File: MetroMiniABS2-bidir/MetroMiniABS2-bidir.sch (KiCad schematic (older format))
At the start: 33 parts, among them CON1 PJ_037A, IC1 MCT6H, J1 RJ45, J2 RJ45, P1 Termination, P2 + 12V (IN) -, P3 In Track Out, P5 - 12V (out) +, SW1 Blue, SW2 Gold, U1 METROMINI, U2 MCP2517, U3 MCP2551, X1 20 Mhz

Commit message: Bidirection (two signals) version of MetroMiniABS2
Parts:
- added P4: CONN_8, ~, symbol CONN_8
- added R1, R13, R14, R6, R7, R8: 330 Ohms, ~, symbol R
- added R15: 10K, ~, symbol R
- added U4: TLC59208F, symbol TLC59208F
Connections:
- wire segments 132 -> 173
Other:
- moved on the sheet: D4, D5, R10, R11, R12, R9, SW1, SW2

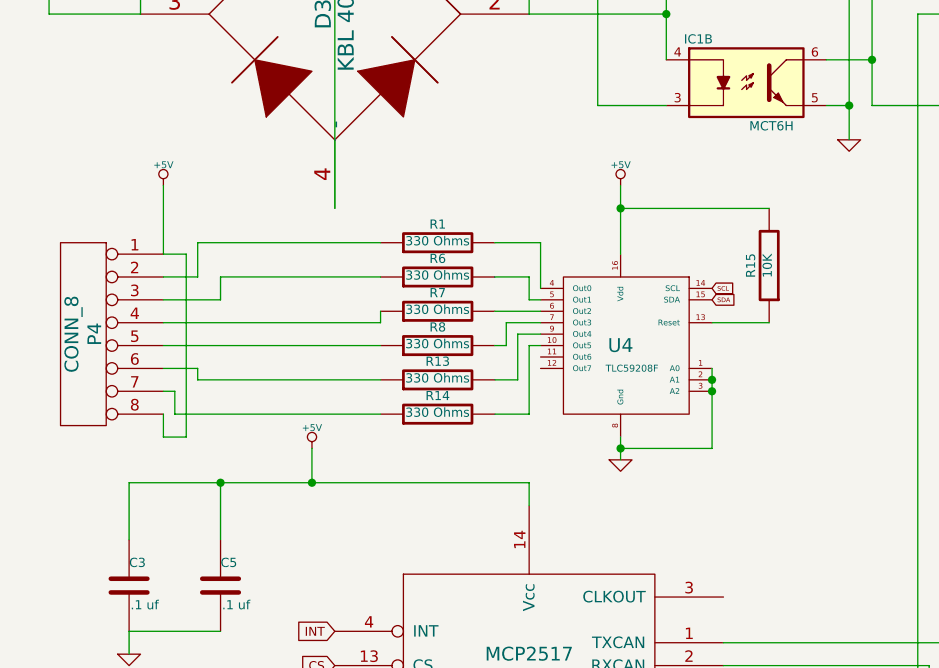
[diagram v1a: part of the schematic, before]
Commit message: Update labels on board
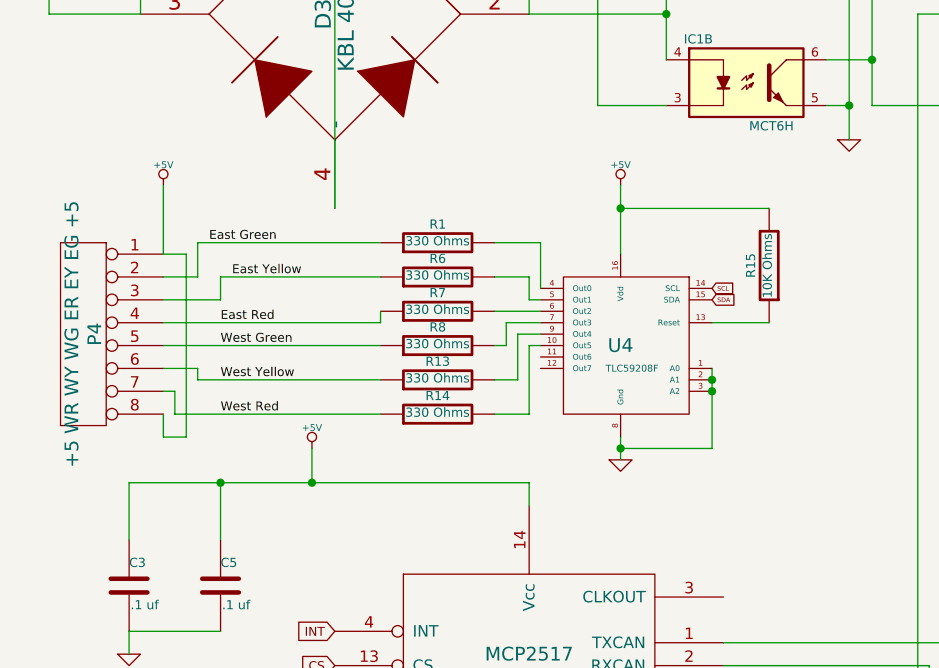
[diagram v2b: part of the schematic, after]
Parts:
- P4: value CONN_8 -> +5 WR WY WG ER EY EG +5
- R15: value 10K -> 10K Ohms
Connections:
- net labels added: East Green, East Red, East Yellow, West Green, West Red, West Yellow
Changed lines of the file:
@@
 Sheet 1 1
 Title ""
-Date "9 jun 2018"
+Date "10 jun 2018"
 Rev ""
 Comp ""
@@
 P 4250 3000
 F 0 "R15" V 4330 3000 40  0000 C CNN
-F 1 "10K" V 4257 3001 40  0000 C CNN
+F 1 "10K Ohms" V 4257 3001 40  0000 C CNN
 F 2 "~" V 4180 3000 30  0000 C CNN
 F 3 "~" H 4250 3000 30  0000 C CNN
@@
 P 1250 3300
 F 0 "P4" V 1200 3300 60  0000 C CNN
-F 1 "CONN_8" V 1300 3300 60  0000 C CNN
+F 1 "+5 WR WY WG ER EY EG +5" V 1300 3300 60  0000 C CNN
 F 2 "~" H 1250 3300 60  0000 C CNN
 F 3 "~" H 1250 3300 60  0000 C CNN
@@
 Connection ~ 4000 3550
 Connection ~ 4000 3500
+Text Label 1800 2900 0    39   ~ 0
+East Green
+Text Label 1900 3050 0    39   ~ 0
+East Yellow
+Text Label 1850 3250 0    39   ~ 0
+East Red
+Text Label 1850 3350 0    39   ~ 0
+West Green
+Text Label 1850 3500 0    39   ~ 0
+West Yellow
+Text Label 1850 3650 0    39   ~ 0
+West Red
 $EndSCHEMATC
